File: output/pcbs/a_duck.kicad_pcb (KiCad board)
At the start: 2 copper layers, 135.1 x 107.9 mm, 38 parts

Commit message: Remove the files put there by the .zip download
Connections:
- S1 pad 2: GND -> pinky_bottom
- S10 pad 2: GND -> ring_home
- S11 pad 2: GND -> ring_top
- S12 pad 2: GND -> ring_top
- S13 pad 2: GND -> middle_bottom
- S14 pad 2: GND -> middle_bottom
- S15 pad 2: GND -> middle_home
- S16 pad 2: GND -> middle_home
- S17 pad 2: GND -> middle_top
- S18 pad 2: GND -> middle_top
- S19 pad 2: GND -> index_bottom
- S2 pad 2: GND -> pinky_bottom
- S20 pad 2: GND -> index_bottom
- S21 pad 2: GND -> index_home
- S22 pad 2: GND -> index_home
- S23 pad 2: GND -> index_top
- S24 pad 2: GND -> index_top
- S25 pad 2: GND -> inner_bottom
- S26 pad 2: GND -> inner_bottom
- S27 pad 2: GND -> inner_home
- S28 pad 2: GND -> inner_home
- S29 pad 2: GND -> inner_top
- S3 pad 2: GND -> pinky_home
- S30 pad 2: GND -> inner_top
- S31 pad 2: GND -> first_only
- S32 pad 2: GND -> first_only
- S33 pad 2: GND -> second_only
- S34 pad 2: GND -> second_only
- S35 pad 2: GND -> third_only
- S36 pad 2: GND -> third_only
- S4 pad 2: GND -> pinky_home
- S5 pad 2: GND -> pinky_top
- S6 pad 2: GND -> pinky_top
- S7 pad 2: GND -> ring_bottom
- S8 pad 2: GND -> ring_bottom
- S9 pad 2: GND -> ring_home

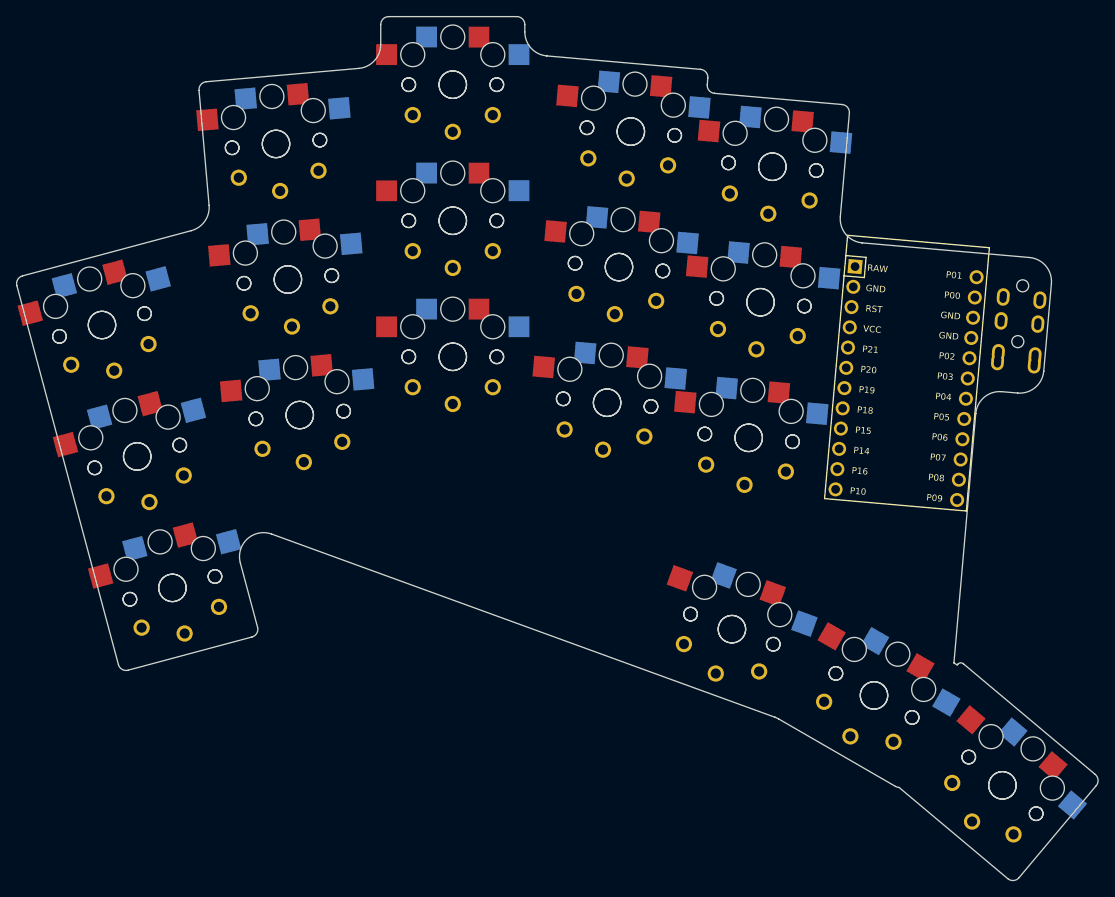
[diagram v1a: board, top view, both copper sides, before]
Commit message: Added diodes correctly, removed the non-hotswap locations for now.  Added wiring 'guide' to help with setting up the wire map
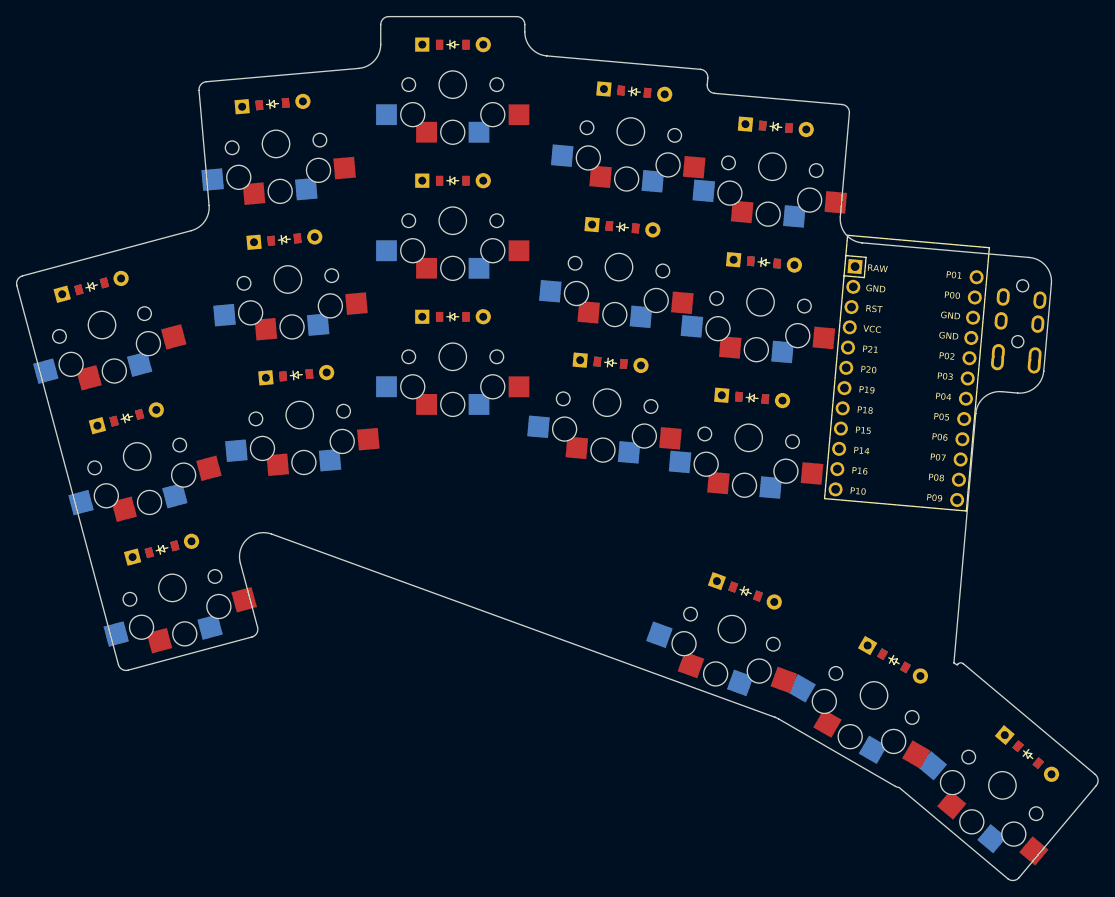
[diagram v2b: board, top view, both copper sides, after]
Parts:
- removed S19, S20, S21, S22, S23, S24, S25, S26, S27, S28, S29, S30, S31, S32, S33, S34, S35, S36: , PG1350
- added D1: , ComboDiode, F.Cu at (12.3, -4.25)
- added D10: , ComboDiode, F.Cu at (68.3, -27.5)
- added D11: , ComboDiode, F.Cu at (69.8, -44.5)
- added D12: , ComboDiode, F.Cu at (71.3, -61.4)
- added D13: , ComboDiode, F.Cu at (86.0, -23.2)
- added D14: , ComboDiode, F.Cu at (87.5, -40.1)
- added D15: , ComboDiode, F.Cu at (89.0, -57.0)
- added D16: , ComboDiode, F.Cu at (85.2, 1.04)
- added D17: , ComboDiode, F.Cu at (103.8, 9.69)
- added D18: , ComboDiode, F.Cu at (120.5, 21.4)
- added D2: , ComboDiode, F.Cu at (7.91, -20.7)
- added D3: , ComboDiode, F.Cu at (3.51, -37.1)
- added D4: , ComboDiode, F.Cu at (29.1, -26.0)
- added D5: , ComboDiode, F.Cu at (27.6, -42.9)
- added D6: , ComboDiode, F.Cu at (26.1, -59.9)
- added D7: , ComboDiode, F.Cu at (48.6, -33.3)
- added D8: , ComboDiode, F.Cu at (48.6, -50.3)
- added D9: , ComboDiode, F.Cu at (48.6, -67.3)
- moved S18 111.3 mm to (117.3, 25.3), turned to 140 degrees
- moved S17 92.7 mm to (101.3, 14.0), turned to 150 degrees
- moved S16 61.8 mm to (83.5, 5.74), turned to 160 degrees
- moved S11 45.5 mm to (69.4, -39.5), turned to 175 degrees
- moved S12 44.4 mm to (70.9, -56.4), turned to 175 degrees
- moved S10 42.7 mm to (67.9, -22.6), turned to 175 degrees
- moved S15 40.5 mm to (88.6, -52.0), turned to 175 degrees
- moved S14 39.0 mm to (87.1, -35.1), turned to 175 degrees
- moved S13 38.3 mm to (85.6, -18.2), turned to 175 degrees
- moved S9 31.9 mm to (48.6, -62.3), turned to 180 degrees
- moved S6 31.4 mm to (26.5, -54.9), turned to 185 degrees
- moved S8 30.9 mm to (48.6, -45.3), turned to 180 degrees
- moved S5 23.9 mm to (28.0, -38.0), turned to 185 degrees
- moved S4 21.0 mm to (29.5, -21.0), turned to 185 degrees
- moved S7 20.5 mm to (48.6, -28.3), turned to 180 degrees
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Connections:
- S1 pad 2: pinky_bottom -> GND
- S10 pad 1: P3 -> P15
- S10 pad 2: ring_home -> GND
- S11 pad 1: P0 -> P14
- S11 pad 2: ring_top -> GND
- S12 pad 1: P0 -> P16
- S12 pad 2: ring_top -> GND
- S13 pad 1: P1 -> P10
- S13 pad 2: middle_bottom -> GND
- S14 pad 1: P1 -> P20
- S14 pad 2: middle_bottom -> GND
- S15 pad 1: P19 -> P21
- S15 pad 2: middle_home -> GND
- S16 pad 1: P19 -> P8
- S16 pad 2: middle_home -> GND
- S17 pad 1: P18 -> P9
- S17 pad 2: middle_top -> GND
- S18 pad 1: P18 -> P10
- S18 pad 2: middle_top -> GND
- S2 pad 1: P7 -> P6
- S2 pad 2: pinky_bottom -> GND
- S3 pad 1: P6 -> P5
- S3 pad 2: pinky_home -> GND
- S4 pad 1: P6 -> P4
- S4 pad 2: pinky_home -> GND
- S5 pad 1: P5 -> P3
- S5 pad 2: pinky_top -> GND
- S6 pad 1: P5 -> P0
- S6 pad 2: pinky_top -> GND
- S7 pad 1: P4 -> P1
- S7 pad 2: ring_bottom -> GND
- S8 pad 1: P4 -> P19
- S8 pad 2: ring_bottom -> GND
- S9 pad 1: P3 -> P18
- S9 pad 2: ring_home -> GND

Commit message: Got the key and diode matrix working!
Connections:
- D1 pad 1: P7 -> pinky_bottom
- D1 pad 2: pinky_bottom -> P16
- D10 pad 1: P15 -> index_bottom
- D10 pad 2: index_bottom -> P16
- D11 pad 1: P14 -> index_home
- D11 pad 2: index_home -> P14
- D12 pad 1: P16 -> index_top
- D12 pad 2: index_top -> P15
- D13 pad 1: P10 -> inner_bottom
- D13 pad 2: inner_bottom -> P16
- D14 pad 1: P20 -> inner_home
- D14 pad 2: inner_home -> P14
- D15 pad 1: P21 -> inner_top
- D15 pad 2: inner_top -> P15
- D16 pad 1: P8 -> first_only
- D16 pad 2: first_only -> P10
- D17 pad 1: P9 -> second_only
- D17 pad 2: second_only -> P10
- D18 pad 1: P10 -> third_only
- D18 pad 2: third_only -> P10
- D2 pad 1: P6 -> pinky_home
- D2 pad 2: pinky_home -> P14
- D3 pad 1: P5 -> pinky_top
- D3 pad 2: pinky_top -> P15
- D4 pad 1: P4 -> ring_bottom
- D4 pad 2: ring_bottom -> P16
- D5 pad 1: P3 -> ring_home
- D5 pad 2: ring_home -> P14
- D6 pad 1: P0 -> ring_top
- D6 pad 2: ring_top -> P15
- D7 pad 1: P1 -> middle_bottom
- D7 pad 2: middle_bottom -> P16
- D8 pad 1: P19 -> middle_home
- D8 pad 2: middle_home -> P14
- D9 pad 1: P18 -> middle_top
- D9 pad 2: middle_top -> P15
- S1 pad 1: P7 -> pinky_bottom
- S1 pad 2: GND -> P9
- S10 pad 1: P15 -> index_bottom
- S10 pad 2: GND -> P6
- S11 pad 1: P14 -> index_home
- S11 pad 2: GND -> P6
- S12 pad 1: P16 -> index_top
- S12 pad 2: GND -> P6
- S13 pad 1: P10 -> inner_bottom
- S13 pad 2: GND -> P5
- S14 pad 1: P20 -> inner_home
- S14 pad 2: GND -> P5
- S15 pad 1: P21 -> inner_top
- S15 pad 2: GND -> P5
- S16 pad 1: P8 -> first_only
- S16 pad 2: GND -> P7
- S17 pad 1: P9 -> second_only
- S17 pad 2: GND -> P6
- S18 pad 1: P10 -> third_only
- S18 pad 2: GND -> P5
- S2 pad 1: P6 -> pinky_home
- S2 pad 2: GND -> P9
- S3 pad 1: P5 -> pinky_top
- S3 pad 2: GND -> P9
- S4 pad 1: P4 -> ring_bottom
- S4 pad 2: GND -> P8
- S5 pad 1: P3 -> ring_home
- S5 pad 2: GND -> P8
- S6 pad 1: P0 -> ring_top
- S6 pad 2: GND -> P8
- S7 pad 1: P1 -> middle_bottom
- S7 pad 2: GND -> P7
- S8 pad 1: P19 -> middle_home
- S8 pad 2: GND -> P7
- S9 pad 1: P18 -> middle_top
- S9 pad 2: GND -> P7

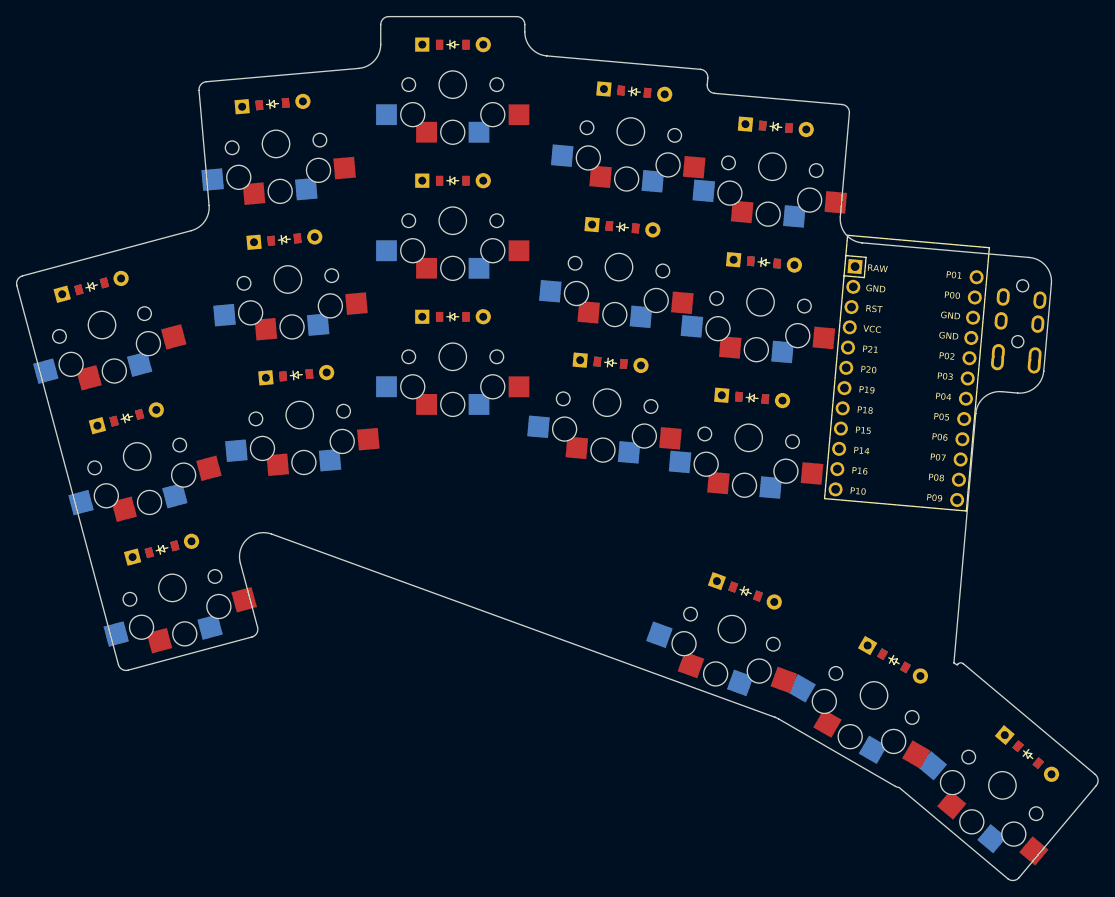
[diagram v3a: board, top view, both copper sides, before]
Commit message: Patch diodes to be SMD only and rotate them for easier routing
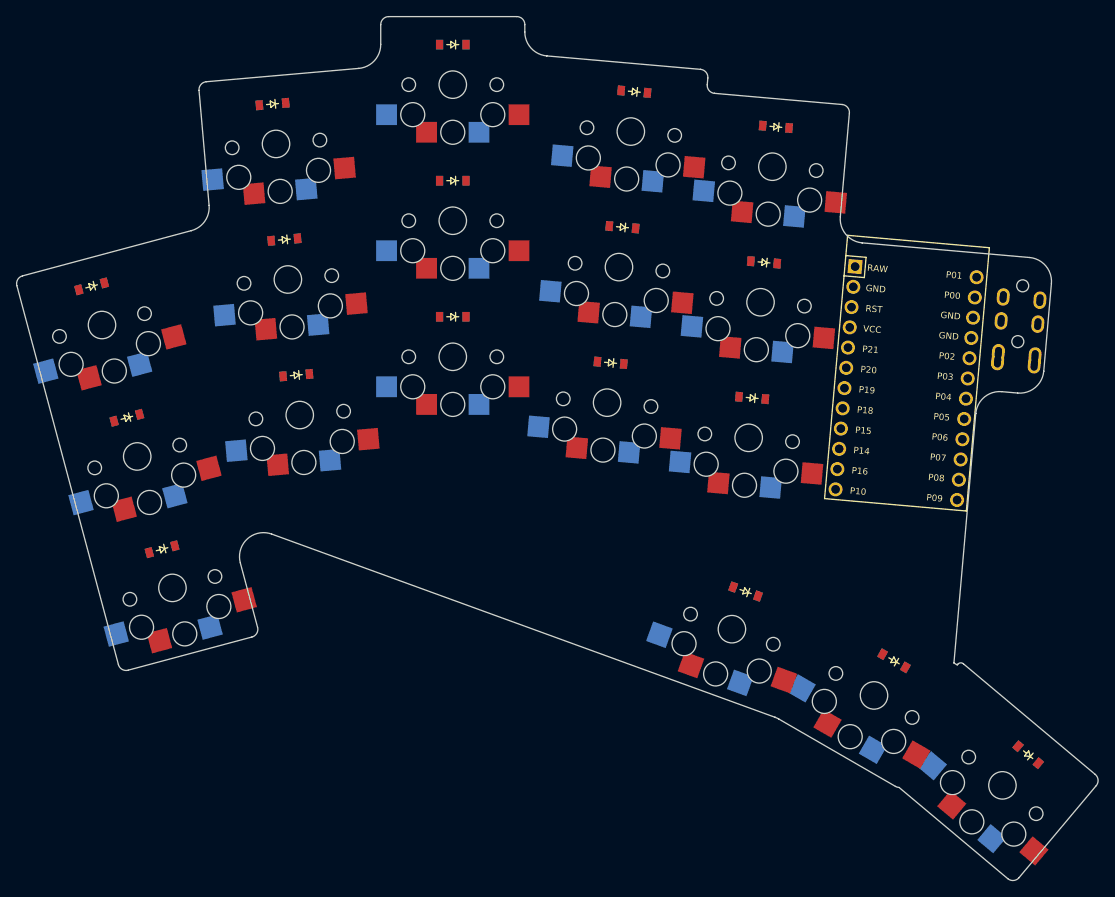
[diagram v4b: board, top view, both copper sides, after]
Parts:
- turned D1 to 195 degrees
- turned D10 to 175 degrees
- turned D11 to 175 degrees
- turned D12 to 175 degrees
- turned D13 to 175 degrees
- turned D14 to 175 degrees
- turned D15 to 175 degrees
- turned D16 to 160 degrees
- turned D17 to 150 degrees
- turned D18 to 140 degrees
- turned D2 to 195 degrees
- turned D3 to 195 degrees
- turned D4 to 185 degrees
- turned D5 to 185 degrees
- turned D6 to 185 degrees
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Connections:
- D1 pad 1: pinky_bottom -> P16
- D1 pad 2: P16 -> pinky_bottom
- D10 pad 1: index_bottom -> P16
- D10 pad 2: P16 -> index_bottom
- D11 pad 1: index_home -> P14
- D11 pad 2: P14 -> index_home
- D12 pad 1: index_top -> P15
- D12 pad 2: P15 -> index_top
- D13 pad 1: inner_bottom -> P16
- D13 pad 2: P16 -> inner_bottom
- D14 pad 1: inner_home -> P14
- D14 pad 2: P14 -> inner_home
- D15 pad 1: inner_top -> P15
- D15 pad 2: P15 -> inner_top
- D16 pad 1: first_only -> P10
- D16 pad 2: P10 -> first_only
- D17 pad 1: second_only -> P10
- D17 pad 2: P10 -> second_only
- D18 pad 1: third_only -> P10
- D18 pad 2: P10 -> third_only
- D2 pad 1: pinky_home -> P14
- D2 pad 2: P14 -> pinky_home
- D3 pad 1: pinky_top -> P15
- D3 pad 2: P15 -> pinky_top
- D4 pad 1: ring_bottom -> P16
- D4 pad 2: P16 -> ring_bottom
- D5 pad 1: ring_home -> P14
- D5 pad 2: P14 -> ring_home
- D6 pad 1: ring_top -> P15
- D6 pad 2: P15 -> ring_top
- D7 pad 1: middle_bottom -> P16
- D7 pad 2: P16 -> middle_bottom
- D8 pad 1: middle_home -> P14
- D8 pad 2: P14 -> middle_home
- D9 pad 1: middle_top -> P15
- D9 pad 2: P15 -> middle_top
